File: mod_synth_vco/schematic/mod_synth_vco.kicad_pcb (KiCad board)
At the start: 2 copper layers, 38.1 x 113 mm, 29 parts, among them J1 Saw, J2 Triangle, J3 Conn_02x08_Odd_Even, J4 Freq CV, J5 PWM CV, J6 Square, U1 TL072, U2 AS3340, U3 TL072

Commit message: Layout PCB
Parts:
- U1, U3: footprint Package_DIP:DIP-8_W7.62mm_LongPads -> Package_DIP:DIP-8_W7.62mm_Socket_LongPads
- moved R12 10.2 mm to (49.5, 105.4), turned to 90 degrees
- moved R14 10.2 mm to (57.1, 95.2), turned to 270 degrees
- moved R2 10.2 mm to (61.0, 95.2), turned to 270 degrees
- moved RV1 1.27 mm to (57.1, 64.8)
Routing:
- net +12V: track 0.00 -> 181.6 mm
- net Net-(R10-Pad1): track 0.00 -> 124.5 mm
- net Net-(R1-Pad1): track 0.00 -> 103.4 mm
- net Net-(R12-Pad1): track 0.00 -> 92.7 mm, vias 0 -> 2
- net Net-(U1-Pad5): track 0.00 -> 77.5 mm
- net Net-(R2-Pad1): track 0.00 -> 76.1 mm
- net Net-(R7-Pad1): track 0.00 -> 72.8 mm
- net Net-(U1-Pad3): track 0.00 -> 67.3 mm
- net -12V: track 0.00 -> 59.7 mm
- net Net-(R6-Pad2): track 0.00 -> 50.8 mm
- net Net-(J5-PadT): track 0.00 -> 43.1 mm
- net Net-(R14-Pad1): track 0.00 -> 34.3 mm
- net Net-(R14-Pad2): track 0.00 -> 27.9 mm
- net Net-(R3-Pad2): track 0.00 -> 27.9 mm
- net Net-(R12-Pad2): track 0.00 -> 27.9 mm
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- added copper zone on F.Cu, net GND

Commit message: Shorten VCO PCB without altering layout yet
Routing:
- removed copper zone on F.Cu, net GND
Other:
- board size 38.1 x 113 mm -> 38.1 x 109.2 mm
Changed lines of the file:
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@@
     )
   )
+  (gr_line (start 76.2 134.62) (end 38.1 134.62) (layer Edge.Cuts) (width 0.05))
+  (gr_line (start 76.2 25.4) (end 76.2 134.62) (layer Edge.Cuts) (width 0.05))
+  (gr_line (start 38.1 25.4) (end 38.1 134.62) (layer Edge.Cuts) (width 0.05))
   (gr_line (start 76.2 25.4) (end 38.1 25.4) (layer Edge.Cuts) (width 0.05))
-  (gr_line (start 76.2 138.43) (end 76.2 25.4) (layer Edge.Cuts) (width 0.05))
-  (gr_line (start 38.1 138.43) (end 76.2 138.43) (layer Edge.Cuts) (width 0.05))
-  (gr_line (start 38.1 25.4) (end 38.1 138.43) (layer Edge.Cuts) (width 0.05))
   (segment (start 60.96 85.01) (end 60.88 85.09) (width 0.25) (layer B.Cu) (net 1))
   (segment (start 49.53 88.9) (end 49.45 88.82) (width 0.25) (layer B.Cu) (net 1))
@@
   (segment (start 69.85 91.44) (end 69.85 85.09) (width 0.25) (layer B.Cu) (net 34))
   (segment (start 69.85 85.09) (end 66.04 85.09) (width 0.25) (layer B.Cu) (net 34))
-  (zone (net 1) (net_name GND) (layer F.Cu) (hatch edge 0.508)
-    (connect_pads (clearance 0.508))
-    (min_thickness 0.254)
-    (fill yes (arc_segments 32) (thermal_gap 0.508) (thermal_bridge_width 0.508))
-    (polygon
-      (pts
-        (xy 38.1 25.4) (xy 76.2 25.4) (xy 76.2 138.43) (xy 38.1 138.43)
-      )
-    )
-  )
 )

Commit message: Update PCB layouts
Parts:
- moved J1 3.81 mm to (69.8, 132.1)
- moved J2 3.81 mm to (57.1, 132.1)
- moved J6 3.81 mm to (44.5, 132.1)
- moved R10 2.54 mm to (41.9, 92.7)
- moved R14 2.54 mm to (57.1, 92.7)
- moved R2 2.54 mm to (61.0, 92.7)
- moved R5 2.54 mm to (53.3, 92.7)
- moved R6 2.54 mm to (45.7, 92.7)
- moved U1 2.54 mm to (61.0, 109.2)
- moved U3 2.54 mm to (48.3, 109.2)
- moved J3 2.54 mm to (68.6, 113.0)
- moved R12 2.54 mm to (49.5, 102.9)
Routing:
- net Net-(R10-Pad1): track 124.5 -> 114.3 mm
- net Net-(R12-Pad1): track 92.7 -> 82.6 mm
- net -12V: track 59.7 -> 53.3 mm
- net GND: track 4.15 -> 0.11 mm, vias 2 -> 0
- net +12V: track 181.6 -> 177.8 mm
- net Net-(R14-Pad1): track 34.3 -> 36.8 mm
- net Net-(R12-Pad2): track 27.9 -> 25.3 mm
- net Net-(U1-Pad3): track 67.3 -> 64.8 mm
- net Net-(R6-Pad2): track 50.8 -> 48.3 mm
- net Net-(R2-Pad1): track 76.1 -> 73.6 mm
- net Net-(J2-PadT): track 14.0 -> 12.7 mm
- net Net-(J6-PadT): track 16.5 -> 15.3 mm
- net Net-(J1-PadT): track 21.6 -> 20.3 mm
- added copper zone on B.Cu, net GND
- added copper zone on F.Cu, net GND

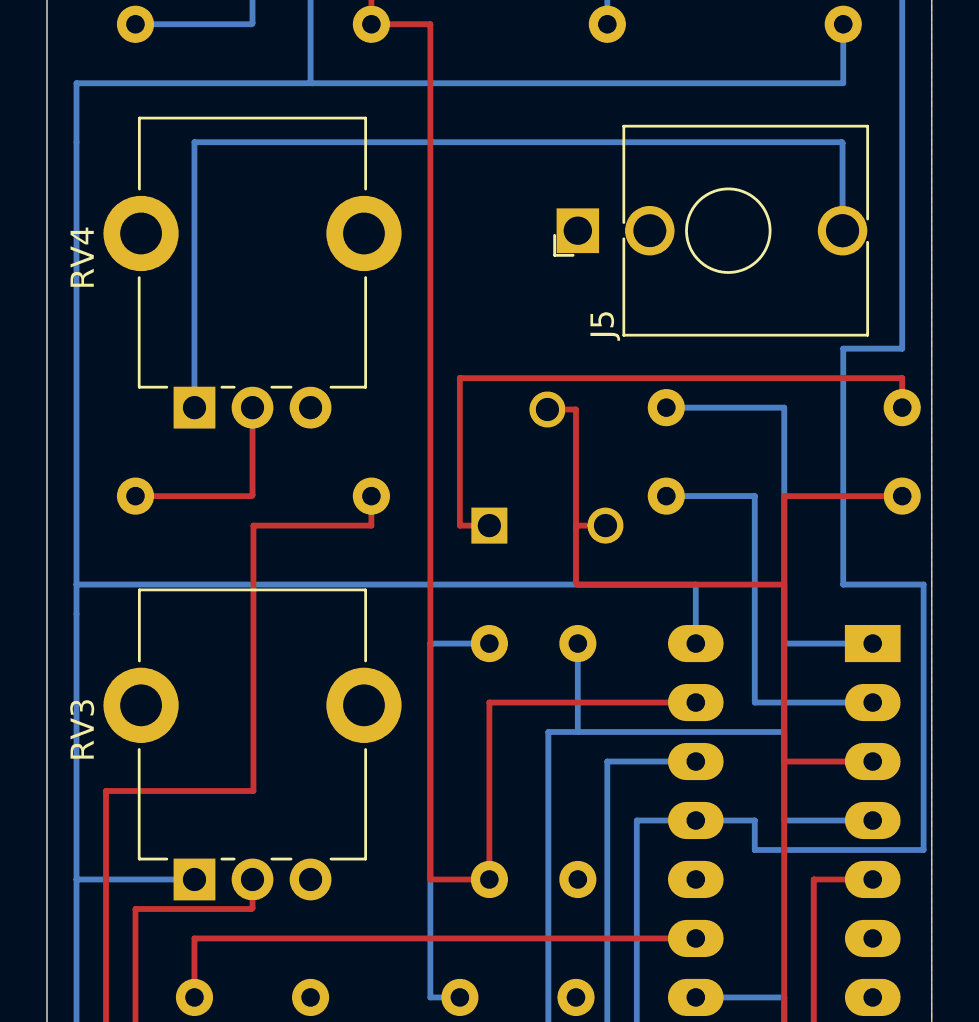
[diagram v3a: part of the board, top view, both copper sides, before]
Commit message: Reverse pulse width knob and CV level
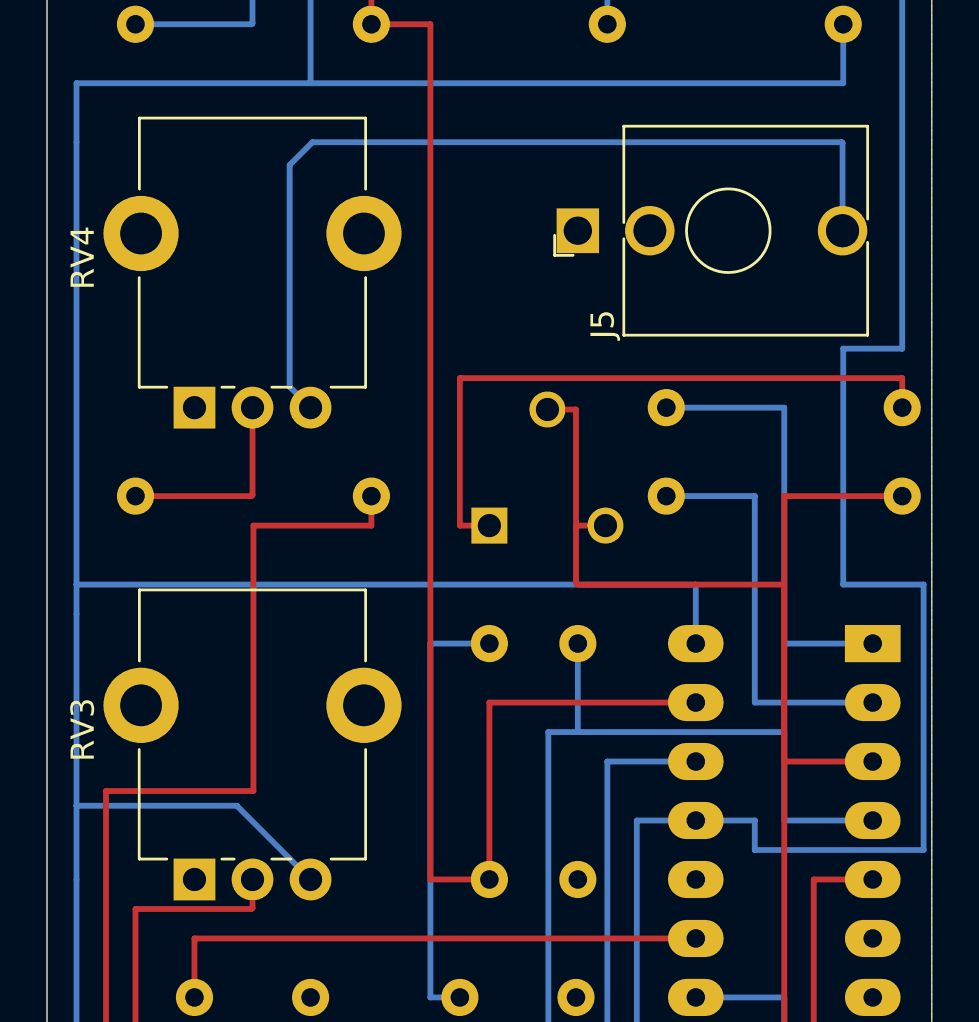
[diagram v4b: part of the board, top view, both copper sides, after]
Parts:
- RV1: value R_POT_TRIM -> 10k
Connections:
- RV3 pad 1: +12V -> GND
- RV3 pad 3: GND -> +12V
- RV4 pad 1: Net-(J5-PadT) -> GND
- RV4 pad 3: GND -> Net-(J5-PadT)
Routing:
- net +12V: track 177.8 -> 184.1 mm
- net Net-(J5-PadT): track 43.1 -> 38.8 mm
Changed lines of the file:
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@@
     (thickness 1.6)
     (drawings 4)
-    (tracks 184)
+    (tracks 188)
     (zones 0)
     (modules 29)
@@
     (pad "" thru_hole circle (at 7.5 7.3 180) (size 3.24 3.24) (drill 1.8) (layers *.Cu *.Mask))
     (pad 3 thru_hole circle (at 0 5 180) (size 1.8 1.8) (drill 1) (layers *.Cu *.Mask)
-      (net 1 GND))
+      (net 16 "Net-(J5-PadT)"))
     (pad 2 thru_hole circle (at 0 2.5 180) (size 1.8 1.8) (drill 1) (layers *.Cu *.Mask)
       (net 29 "Net-(R13-Pad2)"))
     (pad 1 thru_hole rect (at 0 0 180) (size 1.8 1.8) (drill 1) (layers *.Cu *.Mask)
-      (net 16 "Net-(J5-PadT)"))
+      (net 1 GND))
     (model ${KISYS3DMOD}/Potentiometer_THT.3dshapes/Potentiometer_Alpha_RD901F-40-00D_Single_Vertical.wrl
       (at (xyz 0 0 0))
@@
     (pad "" thru_hole circle (at 7.5 7.3 180) (size 3.24 3.24) (drill 1.8) (layers *.Cu *.Mask))
     (pad 3 thru_hole circle (at 0 5 180) (size 1.8 1.8) (drill 1) (layers *.Cu *.Mask)
-      (net 1 GND))
+      (net 13 +12V))
     (pad 2 thru_hole circle (at 0 2.5 180) (size 1.8 1.8) (drill 1) (layers *.Cu *.Mask)
       (net 27 "Net-(R12-Pad2)"))
     (pad 1 thru_hole rect (at 0 0 180) (size 1.8 1.8) (drill 1) (layers *.Cu *.Mask)
-      (net 13 +12V))
+      (net 1 GND))
     (model ${KISYS3DMOD}/Potentiometer_THT.3dshapes/Potentiometer_Alpha_RD901F-40-00D_Single_Vertical.wrl
       (at (xyz 0 0 0))
@@
       (effects (font (size 1 1) (thickness 0.15)) (justify mirror))
     )
-    (fp_text value R_POT_TRIM (at 2.6 -7.4) (layer B.Fab)
+    (fp_text value 10k (at 2.6 -7.4) (layer B.Fab)
       (effects (font (size 1 1) (thickness 0.15)) (justify mirror))
     )
@@
   (segment (start 53.34 114.3) (end 57.15 114.3) (width 0.25) (layer F.Cu) (net 6))
   (segment (start 57.15 114.3) (end 57.15 120.68) (width 0.25) (layer F.Cu) (net 6))
-  (segment (start 39.37 80.01) (end 44.45 80.01) (width 0.25) (layer B.Cu) (net 13))
   (segment (start 66.04 69.85) (end 66.04 67.31) (width 0.25) (layer B.Cu) (net 13))
   (segment (start 66.04 67.31) (end 39.37 67.31) (width 0.25) (layer B.Cu) (net 13))
   (segment (start 39.37 67.31) (end 39.37 68.58) (width 0.25) (layer B.Cu) (net 13))
-  (segment (start 39.37 68.58) (end 39.37 80.01) (width 0.25) (layer B.Cu) (net 13))
   (segment (start 39.37 48.26) (end 39.37 67.31) (width 0.25) (layer B.Cu) (net 13))
   (segment (start 39.37 45.72) (end 39.37 48.26) (width 0.25) (layer B.Cu) (net 13))
@@
   (segment (start 39.37 80.01) (end 39.37 106.68) (width 0.25) (layer B.Cu) (net 13))
   (segment (start 39.37 106.68) (end 40.64 106.68) (width 0.25) (layer B.Cu) (net 13))
+  (segment (start 40.64 106.68) (end 40.64 106.68) (width 0.25) (layer B.Cu) (net 13))
+  (segment (start 40.64 106.68) (end 40.64 109.22) (width 0.25) (layer B.Cu) (net 13))
+  (segment (start 40.64 106.68) (end 53.34 106.68) (width 0.25) (layer B.Cu) (net 13))
+  (segment (start 53.34 106.68) (end 53.34 109.22) (width 0.25) (layer B.Cu) (net 13))
+  (segment (start 53.34 106.68) (end 64.77 106.68) (width 0.25) (layer B.Cu) (net 13))
+  (segment (start 64.77 106.68) (end 64.77 102.87) (width 0.25) (layer B.Cu) (net 13))
+  (segment (start 64.77 102.87) (end 68.58 102.87) (width 0.25) (layer B.Cu) (net 13))
+  (segment (start 68.58 102.87) (end 71.12 102.87) (width 0.25) (layer B.Cu) (net 13))
+  (segment (start 46.275 76.835) (end 39.37 76.835) (width 0.25) (layer B.Cu) (net 13))
+  (segment (start 49.45 80.01) (end 46.275 76.835) (width 0.25) (layer B.Cu) (net 13))
+  (segment (start 39.37 68.58) (end 39.37 76.835) (width 0.25) (layer B.Cu) (net 13))
+  (segment (start 39.37 76.835) (end 39.37 80.01) (width 0.25) (layer B.Cu) (net 13))
   (segment (start 71.12 113.03) (end 68.58 113.03) (width 0.25) (layer F.Cu) (net 14))
   (segment (start 68.58 113.03) (end 64.77 113.03) (width 0.25) (layer F.Cu) (net 14))
@@
   (segment (start 72.36 52.07) (end 72.36 48.29) (width 0.25) (layer B.Cu) (net 16))
   (segment (start 72.36 48.29) (end 72.33 48.26) (width 0.25) (layer B.Cu) (net 16))
-  (segment (start 72.33 48.26) (end 44.45 48.26) (width 0.25) (layer B.Cu) (net 16))
-  (segment (start 44.45 48.26) (end 44.45 59.69) (width 0.25) (layer B.Cu) (net 16))
+  (segment (start 48.550001 58.790001) (end 48.550001 49.239999) (width 0.25) (layer B.Cu) (net 16))
+  (segment (start 49.45 59.69) (end 48.550001 58.790001) (width 0.25) (layer B.Cu) (net 16))
+  (segment (start 48.550001 49.239999) (end 49.53 48.26) (width 0.25) (layer B.Cu) (net 16))
+  (segment (start 72.33 48.26) (end 49.53 48.26) (width 0.25) (layer B.Cu) (net 16))
   (segment (start 44.45 120.68) (end 44.45 111.76) (width 0.25) (layer F.Cu) (net 17))
   (segment (start 44.45 111.76) (end 48.26 111.76) (width 0.25) (layer F.Cu) (net 17))
@@
   (segment (start 75.84999 67.31) (end 72.39 67.31) (width 0.25) (layer B.Cu) (net 18))
   (segment (start 72.39 67.31) (end 72.39 57.15) (width 0.25) (layer B.Cu) (net 18))
+  (segment (start 63.5 77.47) (end 63.5 96.52) (width 0.25) (layer B.Cu) (net 18))
+  (segment (start 63.5 96.52) (end 53.34 96.52) (width 0.25) (layer B.Cu) (net 18))
+  (segment (start 53.34 96.52) (end 53.34 92.71) (width 0.25) (layer B.Cu) (net 18))
   (segment (start 69.85 91.44) (end 69.85 74.93) (width 0.25) (layer F.Cu) (net 19))
   (segment (start 69.85 74.93) (end 73.66 74.93) (width 0.25) (layer F.Cu) (net 19))
@@
   (segment (start 68.58 63.5) (end 68.58 72.39) (width 0.25) (layer B.Cu) (net 22))
   (segment (start 62.23 74.93) (end 66.04 74.93) (width 0.25) (layer B.Cu) (net 23))
+  (segment (start 62.23 74.93) (end 62.23 90.17) (width 0.25) (layer B.Cu) (net 23))
+  (segment (start 62.23 90.17) (end 52.07 90.17) (width 0.25) (layer B.Cu) (net 23))
+  (segment (start 52.07 90.17) (end 52.07 96.52) (width 0.25) (layer B.Cu) (net 23))
+  (segment (start 52.07 96.52) (end 45.72 96.52) (width 0.25) (layer B.Cu) (net 23))
+  (segment (start 45.72 96.52) (end 45.72 102.87) (width 0.25) (layer B.Cu) (net 23))
   (segment (start 66.04 72.39) (end 66.44 72.39) (width 0.25) (layer B.Cu) (net 24))
   (segment (start 62.23 39.37) (end 52.07 39.37) (width 0.25) (layer F.Cu) (net 24))
@@
   (segment (start 58.42 100.33) (end 52.07 100.33) (width 0.25) (layer F.Cu) (net 26))
   (segment (start 52.07 100.33) (end 52.07 104.14) (width 0.25) (layer F.Cu) (net 26))
+  (segment (start 59.69 73.66) (end 59.69 88.9) (width 0.25) (layer B.Cu) (net 26))
+  (segment (start 59.69 88.9) (end 41.91 88.9) (width 0.25) (layer B.Cu) (net 26))
+  (segment (start 41.91 88.9) (end 41.91 92.71) (width 0.25) (layer B.Cu) (net 26))
   (segment (start 46.91 81.28) (end 41.91 81.28) (width 0.25) (layer F.Cu) (net 27))
   (segment (start 46.95 80.01) (end 46.95 81.24) (width 0.25) (layer F.Cu) (net 27))
@@
   (segment (start 41.91 90.17) (end 49.53 90.17) (width 0.25) (layer F.Cu) (net 27))
   (segment (start 49.53 90.17) (end 49.53 92.71) (width 0.25) (layer F.Cu) (net 27))
-  (segment (start 40.64 106.68) (end 40.64 106.68) (width 0.25) (layer B.Cu) (net 13))
-  (segment (start 40.64 106.68) (end 40.64 109.22) (width 0.25) (layer B.Cu) (net 13))
-  (segment (start 40.64 106.68) (end 53.34 106.68) (width 0.25) (layer B.Cu) (net 13))
-  (segment (start 53.34 106.68) (end 53.34 109.22) (width 0.25) (layer B.Cu) (net 13))
-  (segment (start 53.34 106.68) (end 64.77 106.68) (width 0.25) (layer B.Cu) (net 13))
-  (segment (start 64.77 106.68) (end 64.77 102.87) (width 0.25) (layer B.Cu) (net 13))
-  (segment (start 64.77 102.87) (end 68.58 102.87) (width 0.25) (layer B.Cu) (net 13))
-  (segment (start 68.58 102.87) (end 71.12 102.87) (width 0.25) (layer B.Cu) (net 13))
-  (segment (start 63.5 77.47) (end 63.5 96.52) (width 0.25) (layer B.Cu) (net 18))
-  (segment (start 63.5 96.52) (end 53.34 96.52) (width 0.25) (layer B.Cu) (net 18))
-  (segment (start 53.34 96.52) (end 53.34 92.71) (width 0.25) (layer B.Cu) (net 18))
-  (segment (start 62.23 74.93) (end 62.23 90.17) (width 0.25) (layer B.Cu) (net 23))
-  (segment (start 62.23 90.17) (end 52.07 90.17) (width 0.25) (layer B.Cu) (net 23))
-  (segment (start 52.07 90.17) (end 52.07 96.52) (width 0.25) (layer B.Cu) (net 23))
-  (segment (start 52.07 96.52) (end 45.72 96.52) (width 0.25) (layer B.Cu) (net 23))
-  (segment (start 45.72 96.52) (end 45.72 102.87) (width 0.25) (layer B.Cu) (net 23))
-  (segment (start 59.69 73.66) (end 59.69 88.9) (width 0.25) (layer B.Cu) (net 26))
-  (segment (start 59.69 88.9) (end 41.91 88.9) (width 0.25) (layer B.Cu) (net 26))
-  (segment (start 41.91 88.9) (end 41.91 92.71) (width 0.25) (layer B.Cu) (net 26))
   (segment (start 46.99 64.77) (end 52.07 64.77) (width 0.25) (layer F.Cu) (net 28))
   (segment (start 46.99 76.2) (end 46.99 64.77) (width 0.25) (layer F.Cu) (net 28))

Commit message: Connect J1 to GND
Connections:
- J1 pad S: Net-(J1-PadS) -> GND
